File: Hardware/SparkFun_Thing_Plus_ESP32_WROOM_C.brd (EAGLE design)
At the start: 22.9 x 58.7 mm, 110 parts, among them J2 MICRO-SDFRICTION, J3 QWIIC_RA, J5 THING_PLUS_LOGICAL, Q2 MBT3904DW1T1, Q3 20V/4.2A/52mΩ/1.4W, U1 MCP73831, U2 ESP-WROOM-3232D-NARROW, U3 XC6222B331MR-G, U4 MAX17048, U5 XC6222B331MR-G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

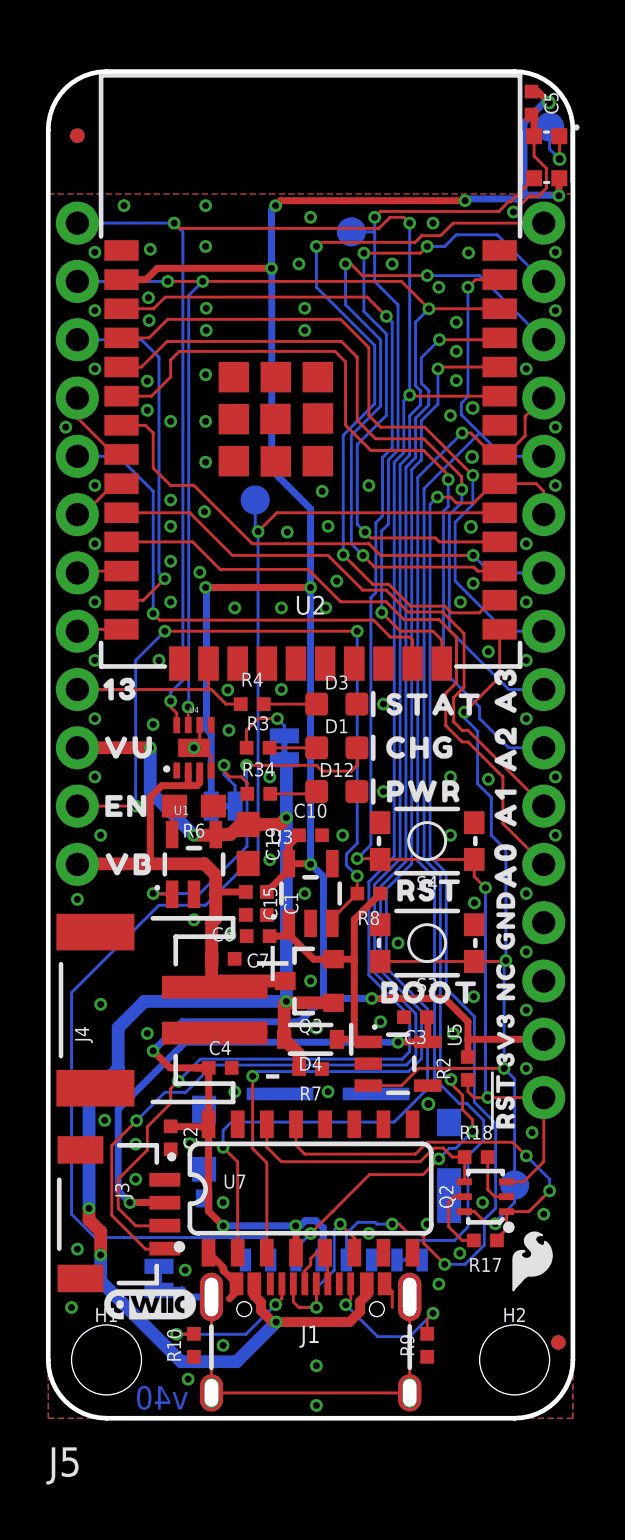
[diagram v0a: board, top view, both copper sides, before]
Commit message: Increase board length to sit on 0.05" grid.
Originally had only increased by 0.01", however was told that customers prefer 0.05" increments for designing around.
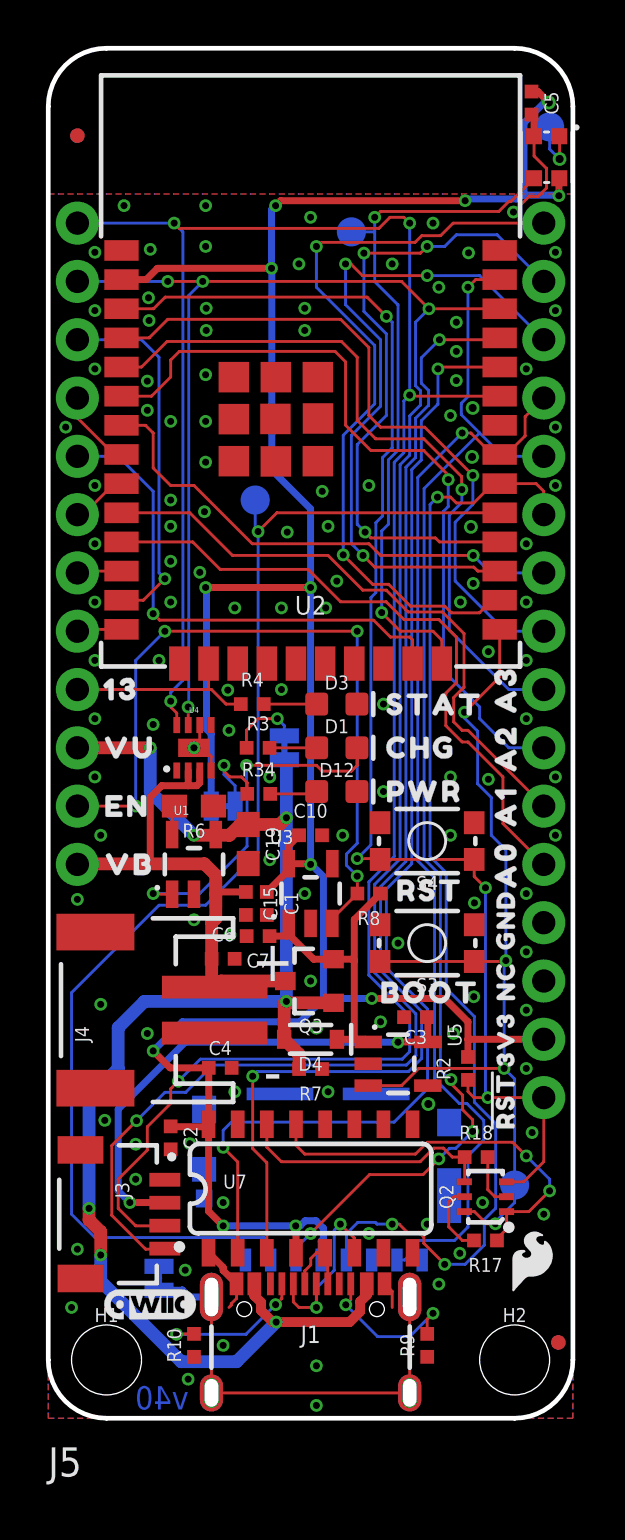
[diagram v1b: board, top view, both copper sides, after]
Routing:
- net 3.3V: track 119.1 -> 118.3 mm
- net GND: track 11.8 -> 12.5 mm
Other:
- board size 22.9 x 58.7 mm -> 22.9 x 59.7 mm

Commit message: Update BOM for cap mismatch.
Accidentally placed C4/C5 in the wrong spot. Made the change in schematic so no board reorder is necessary.
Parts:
- C4: value 0.1uF -> 10uF
- C5: value 10uF -> 0.1uF
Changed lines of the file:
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@@
 <drawing>
 <settings>
-<setting alwaysvectorfont="yes"/>
+<setting alwaysvectorfont="no"/>
 <setting keepoldvectorfont="yes"/>
 <setting verticaltext="up"/>
 </settings>
-<grid distance="0.01" unitdist="inch" unit="inch" style="lines" multiple="1" display="yes" altdistance="0.001" altunitdist="inch" altunit="inch"/>
+<grid distance="0.1" unitdist="mm" unit="mm" style="lines" multiple="1" display="yes" altdistance="0.01" altunitdist="mm" altunit="mm"/>
 <layers>
 <layer number="1" name="Top/Horz" color="4" fill="1" visible="yes" active="yes"/>
@@
 <attribute name="VALUE" x="16.002" y="18.0372" size="0.6096" layer="27" font="vector" ratio="20" rot="R180" align="top-center"/>
 </element>
-<element name="C4" library="SparkFun-Capacitors" package="0402-TIGHT" value="0.1uF" x="7.493" y="15.2654" smashed="yes">
+<element name="C4" library="SparkFun-Capacitors" package="0402-TIGHT" value="10uF" x="7.493" y="15.2654" smashed="yes">
 <attribute name="NAME" x="7.493" y="15.8274" size="0.6096" layer="25" font="vector" ratio="20" align="bottom-center"/>
-<attribute name="PROD_ID" value="CAP-14993" x="8.763" y="15.2654" size="1.778" layer="27" font="vector" ratio="15" display="off"/>
-<attribute name="VALUE" x="7.493" y="14.7034" size="0.6096" layer="27" font="vector" ratio="20" align="top-center"/>
+<attribute name="PROD_ID" value="CAP-14848" x="8.763" y="15.2654" size="1.778" layer="27" font="vector" ratio="15" display="off"/>
+<attribute name="VALUE" value="10uF" x="7.493" y="14.7034" size="0.6096" layer="27" font="vector" ratio="20" align="top-center"/>
 </element>
 <element name="D5" library="SparkFun-LED" package="WS2812-2020" value="WS2812" x="21.717" y="54.9402" smashed="yes" rot="R90">
 <attribute name="PROD_ID" value="DIO-15591" x="21.717" y="54.9402" size="1.778" layer="27" font="vector" ratio="15" rot="R90" display="off"/>
 </element>
-<element name="C5" library="SparkFun-Capacitors" package="0402-TIGHT" value="10uF" x="21.0566" y="57.3024" smashed="yes" rot="R270">
+<element name="C5" library="SparkFun-Capacitors" package="0402-TIGHT" value="0.1uF" x="21.0566" y="57.3024" smashed="yes" rot="R270">
 <attribute name="NAME" x="21.6186" y="57.3024" size="0.6096" layer="25" font="vector" ratio="20" rot="R270" align="bottom-center"/>
-<attribute name="PROD_ID" value="CAP-14848" x="21.0566" y="56.0324" size="1.778" layer="27" font="vector" ratio="15" rot="R270" display="off"/>
-<attribute name="VALUE" value="10uF" x="20.4946" y="57.3024" size="0.6096" layer="27" font="vector" ratio="20" rot="R270" align="top-center"/>
+<attribute name="PROD_ID" value="CAP-14993" x="21.0566" y="56.0324" size="1.778" layer="27" font="vector" ratio="15" rot="R270" display="off"/>
+<attribute name="VALUE" value="0.1uF" x="20.4946" y="57.3024" size="0.6096" layer="27" font="vector" ratio="20" rot="R270" align="top-center"/>
 </element>
 <element name="U$72" library="output" package="#17#TX#0" value="" x="21.082" y="49.53" smashed="yes" rot="MR0"/>

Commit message: Swap VREG IC
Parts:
- U3, U5: value XC6222B331MR-G -> 3.3V
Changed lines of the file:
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@@
 <attribute name="VALUE" x="11.43" y="29.21" size="0.6096" layer="28" font="vector" ratio="20" rot="MR270" align="top-center"/>
 </element>
-<element name="U3" library="SparkFun-IC-Power" package="SOT23-5" value="XC6222B331MR-G" x="11.43" y="22.86" smashed="yes">
-<attribute name="IOUT" value="700mA" x="11.43" y="22.86" size="1.778" layer="27" display="off"/>
+<element name="U3" library="SparkFun-IC-Power" package="SOT23-5" value="3.3V" x="11.43" y="22.86" smashed="yes">
 <attribute name="NAME" x="9.652" y="25.019" size="0.6096" layer="25" ratio="20"/>
-<attribute name="PROD_ID" value="VREG-16775" x="11.43" y="22.86" size="1.778" layer="27" display="off"/>
-<attribute name="VALUE" x="9.652" y="20.066" size="0.6096" layer="27" ratio="20"/>
-<attribute name="VOUT" value="3.3V" x="11.43" y="22.86" size="1.778" layer="27" display="off"/>
+<attribute name="PROD_ID" value="VREG-12457" x="11.43" y="22.86" size="1.778" layer="27" display="off"/>
+<attribute name="VALUE" value="3.3V" x="9.652" y="20.066" size="0.6096" layer="27" ratio="20"/>
 </element>
-<element name="U5" library="SparkFun-IC-Power" package="SOT23-5" value="XC6222B331MR-G" x="15.24" y="15.4432" smashed="yes" rot="R270">
-<attribute name="IOUT" value="700mA" x="15.24" y="15.4432" size="1.778" layer="27" rot="R270" display="off"/>
+<element name="U5" library="SparkFun-IC-Power" package="SOT23-5" value="3.3V" x="15.24" y="15.4432" smashed="yes" rot="R270">
 <attribute name="NAME" x="17.399" y="17.2212" size="0.6096" layer="25" ratio="20" rot="R270"/>
-<attribute name="PROD_ID" value="VREG-16775" x="15.24" y="15.4432" size="1.778" layer="27" rot="R270" display="off"/>
-<attribute name="VALUE" x="12.446" y="17.2212" size="0.6096" layer="27" ratio="20" rot="R270"/>
-<attribute name="VOUT" value="3.3V" x="15.24" y="15.4432" size="1.778" layer="27" rot="R270" display="off"/>
+<attribute name="PROD_ID" value="VREG-12457" x="15.24" y="15.4432" size="1.778" layer="27" rot="R270" display="off"/>
+<attribute name="VALUE" value="3.3V" x="12.446" y="17.2212" size="0.6096" layer="27" ratio="20" rot="R270"/>
 </element>
 <element name="J2" library="SparkFun-Connectors" package="MICROSD_TINY" value="MICRO-SDFRICTION" x="12.1412" y="10.7442" smashed="yes" rot="MR0">
